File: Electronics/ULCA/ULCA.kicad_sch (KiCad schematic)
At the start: 0 parts

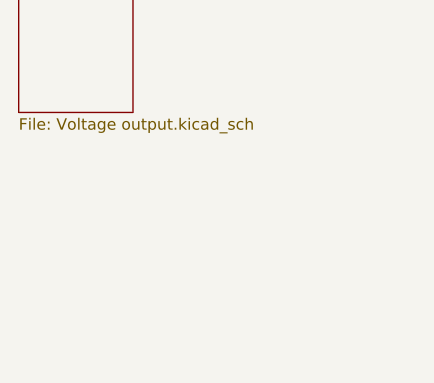
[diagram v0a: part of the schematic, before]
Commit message: Create simulation of ULCA with parasitic capacitances
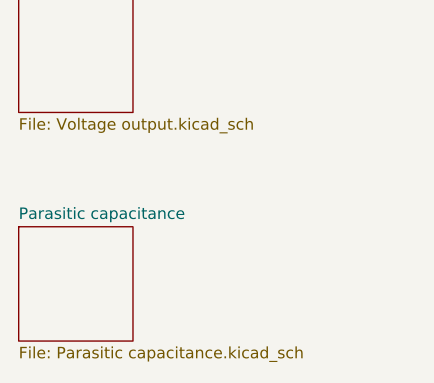
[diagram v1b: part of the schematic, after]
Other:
- added sheet Parasitic capacitance (Parasitic capacitance.kicad_sch)
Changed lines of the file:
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@@
 		(at 127 88.9)
 		(size 12.7 12.7)
-		(exclude_from_sim no)
+		(exclude_from_sim yes)
 		(in_bom yes)
 		(on_board yes)
@@
 				)
 			)
+		)
+	)
+	(sheet
+		(at 127 114.3)
+		(size 12.7 12.7)
+		(exclude_from_sim no)
+		(in_bom yes)
+		(on_board yes)
+		(dnp no)
+		(fields_autoplaced yes)
+		(stroke
+			(width 0.1524)
+			(type solid)
+		)
+		(fill
+			(color 0 0 0 0)
+		)
+		(property "Sheetname" "Parasitic capacitance"
+			(at 127 113.5884 0)
+			(show_name no)
+			(do_not_autoplace no)
+			(effects
+				(font
+					(size 1.27 1.27)
+				)
+				(justify left bottom)
+			)
+		)
+		(property "Sheetfile" "Parasitic capacitance.kicad_sch"
+			(at 127 127.5846 0)
+			(show_name no)
+			(do_not_autoplace no)
+			(effects
+				(font
+					(size 1.27 1.27)
+				)
+				(justify left top)
+			)
+		)
+		(instances
+			(project "ULCA"
+				(path "/ad97f578-e6f0-4b7f-b1a4-b9871390a9f6"
+					(page "3")
+				)
+			)

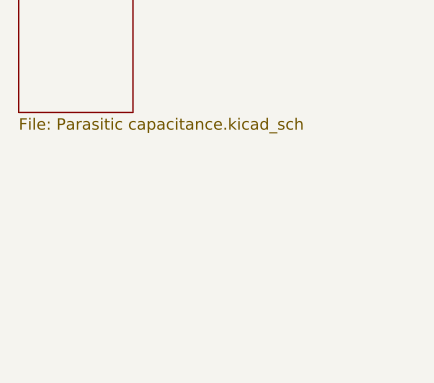
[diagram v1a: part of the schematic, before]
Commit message: Achieve good specifications under unrealistic conditions for the ULCA
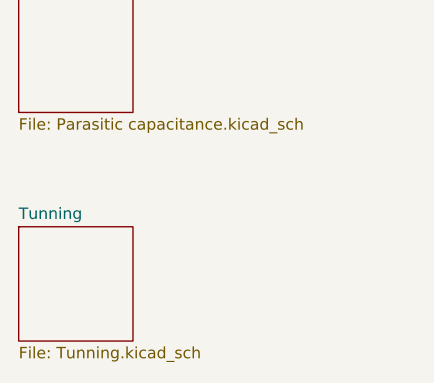
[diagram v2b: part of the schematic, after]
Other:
- added sheet Tunning (Tunning.kicad_sch)
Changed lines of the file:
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@@
 	(paper "A4")
+	(sheet
+		(at 127 139.7)
+		(size 12.7 12.7)
+		(exclude_from_sim no)
+		(in_bom yes)
+		(on_board yes)
+		(dnp no)
+		(fields_autoplaced yes)
+		(stroke
+			(width 0.1524)
+			(type solid)
+		)
+		(fill
+			(color 0 0 0 0)
+		)
+		(property "Sheetname" "Tunning"
+			(at 127 138.9884 0)
+			(show_name no)
+			(do_not_autoplace no)
+			(effects
+				(font
+					(size 1.27 1.27)
+				)
+				(justify left bottom)
+			)
+		)
+		(property "Sheetfile" "Tunning.kicad_sch"
+			(at 127 152.9846 0)
+			(show_name no)
+			(do_not_autoplace no)
+			(effects
+				(font
+					(size 1.27 1.27)
+				)
+				(justify left top)
+			)
+		)
+		(instances
+			(project "ULCA"
+				(path "/ad97f578-e6f0-4b7f-b1a4-b9871390a9f6"
+					(page "4")
+				)
+			)
+		)
+	)
 	(sheet
 		(at 127 88.9)
@@
 		(at 127 114.3)
 		(size 12.7 12.7)
-		(exclude_from_sim no)
+		(exclude_from_sim yes)
 		(in_bom yes)
 		(on_board yes)

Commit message: Create an okayish tunned ULCA
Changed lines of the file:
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@@
 	(paper "A4")
 	(sheet
-		(at 127 139.7)
+		(at 38.1 88.9)
 		(size 12.7 12.7)
 		(exclude_from_sim no)
@@
 		)
 		(property "Sheetname" "Tunning"
-			(at 127 138.9884 0)
+			(at 38.1 88.1884 0)
 			(show_name no)
 			(do_not_autoplace no)
@@
 		)
 		(property "Sheetfile" "Tunning.kicad_sch"
-			(at 127 152.9846 0)
+			(at 38.1 102.1846 0)
 			(show_name no)
 			(do_not_autoplace no)
@@
 	)
 	(sheet
-		(at 127 88.9)
+		(at 38.1 38.1)
 		(size 12.7 12.7)
 		(exclude_from_sim yes)
@@
 		)
 		(property "Sheetname" "Voltage output"
-			(at 127 88.1884 0)
+			(at 38.1 37.3884 0)
 			(show_name no)
 			(do_not_autoplace no)
@@
 		)
 		(property "Sheetfile" "Voltage output.kicad_sch"
-			(at 127 102.1846 0)
+			(at 38.1 51.3846 0)
 			(show_name no)
 			(do_not_autoplace no)
@@
 	)
 	(sheet
-		(at 127 114.3)
+		(at 38.1 63.5)
 		(size 12.7 12.7)
 		(exclude_from_sim yes)
@@
 		)
 		(property "Sheetname" "Parasitic capacitance"
-			(at 127 113.5884 0)
+			(at 38.1 62.7884 0)
 			(show_name no)
 			(do_not_autoplace no)
@@
 		)
 		(property "Sheetfile" "Parasitic capacitance.kicad_sch"
-			(at 127 127.5846 0)
+			(at 38.1 76.7846 0)
 			(show_name no)
 			(do_not_autoplace no)
